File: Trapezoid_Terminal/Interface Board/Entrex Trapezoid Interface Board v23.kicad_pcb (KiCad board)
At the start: 2 copper layers, 169.1 x 191 mm, 101 parts, among them P15 Conn_02x40_Odd_Even_Shielded, SW1 SW_DIP_x08

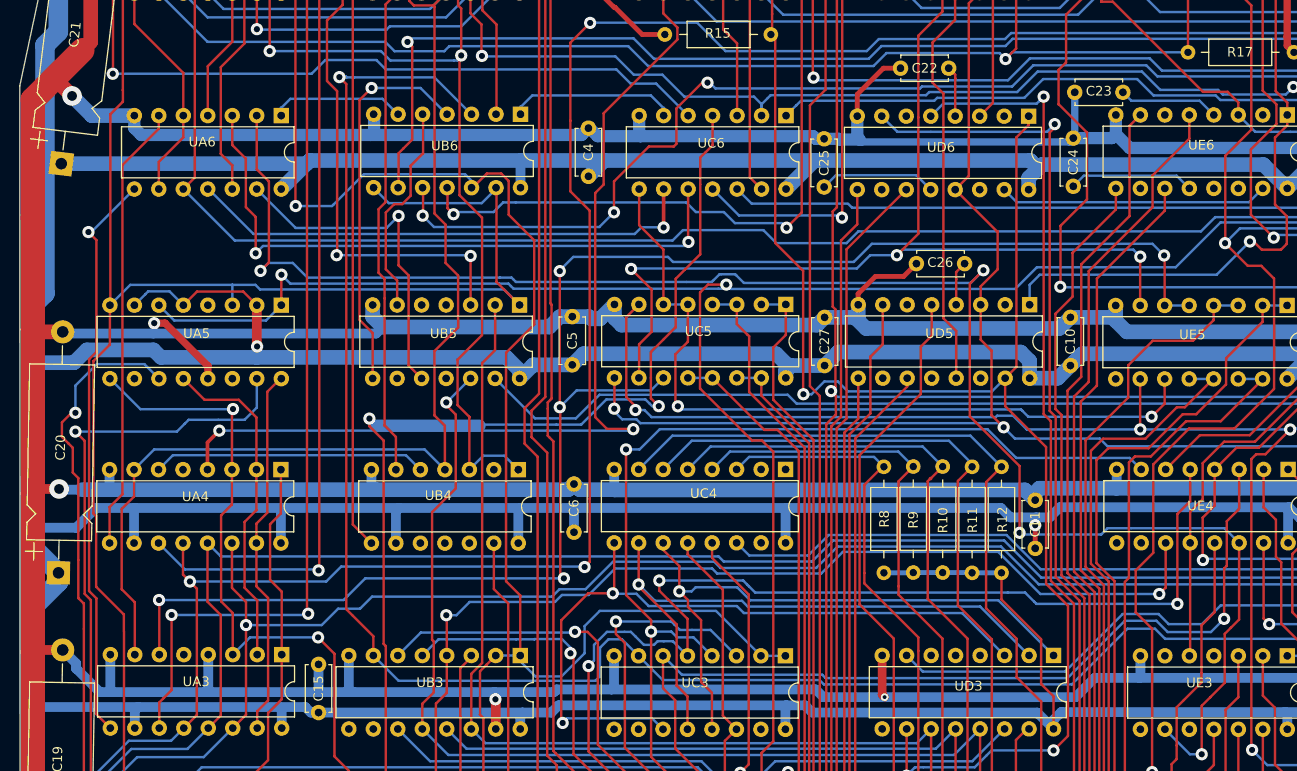
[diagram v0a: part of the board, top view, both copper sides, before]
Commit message: fix interface board errors
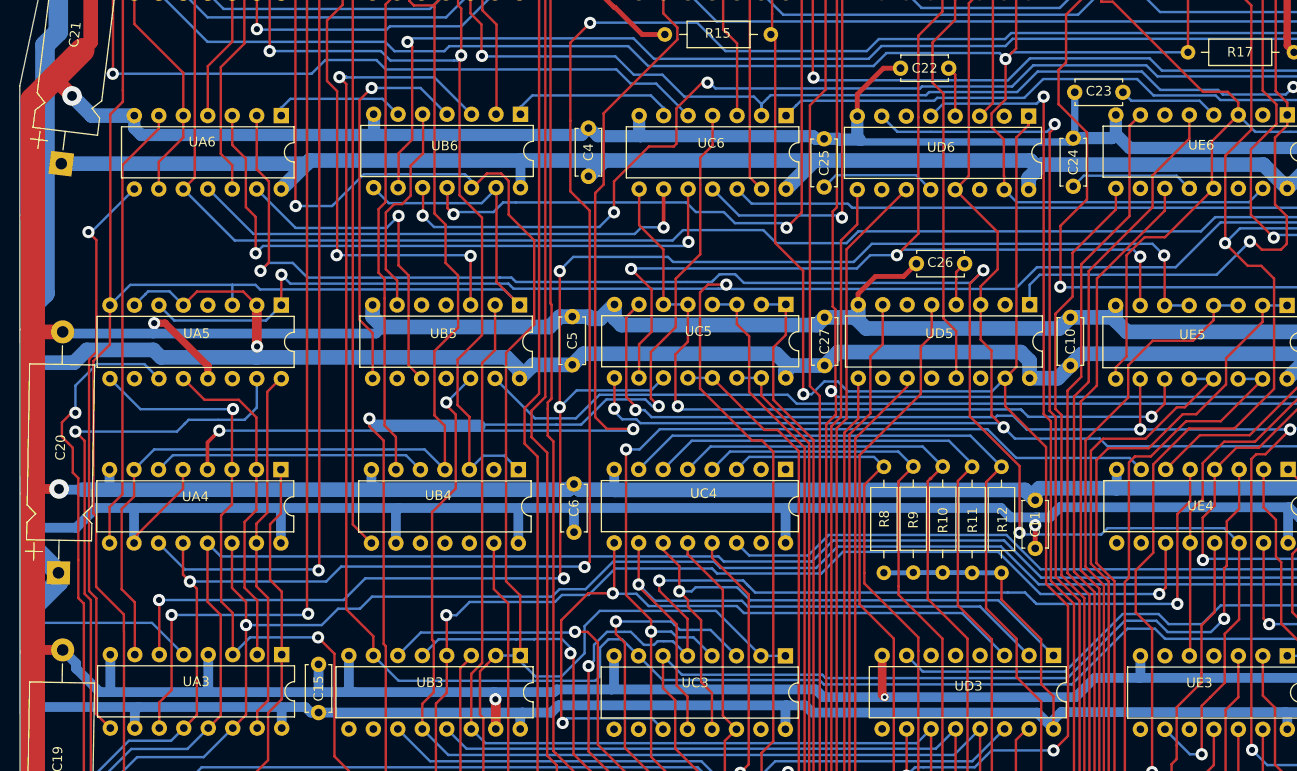
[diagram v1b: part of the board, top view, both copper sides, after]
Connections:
- UA3 pad 5: /XX(UA3P5) -> VCC
- UA4 pad 5: /XX(UA4P5) -> VCC
- UD6 pad 15: u16_15 -> u4_3
- UE5 pad 9: /XX(UE5P9) -> u4_2
- UE6 pad 13: unconnected-(UE6-2STRB-Pad13) -> u4_2
- UE6 pad 15: u16_15 -> u4_3
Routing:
- net u4_3: track 154.5 -> 197.2 mm
- net u4_2: track 214.8 -> 248.9 mm
- net u16_15: track 28.0 -> 0.00 mm
- net VCC: track 1844.7 -> 1871.5 mm

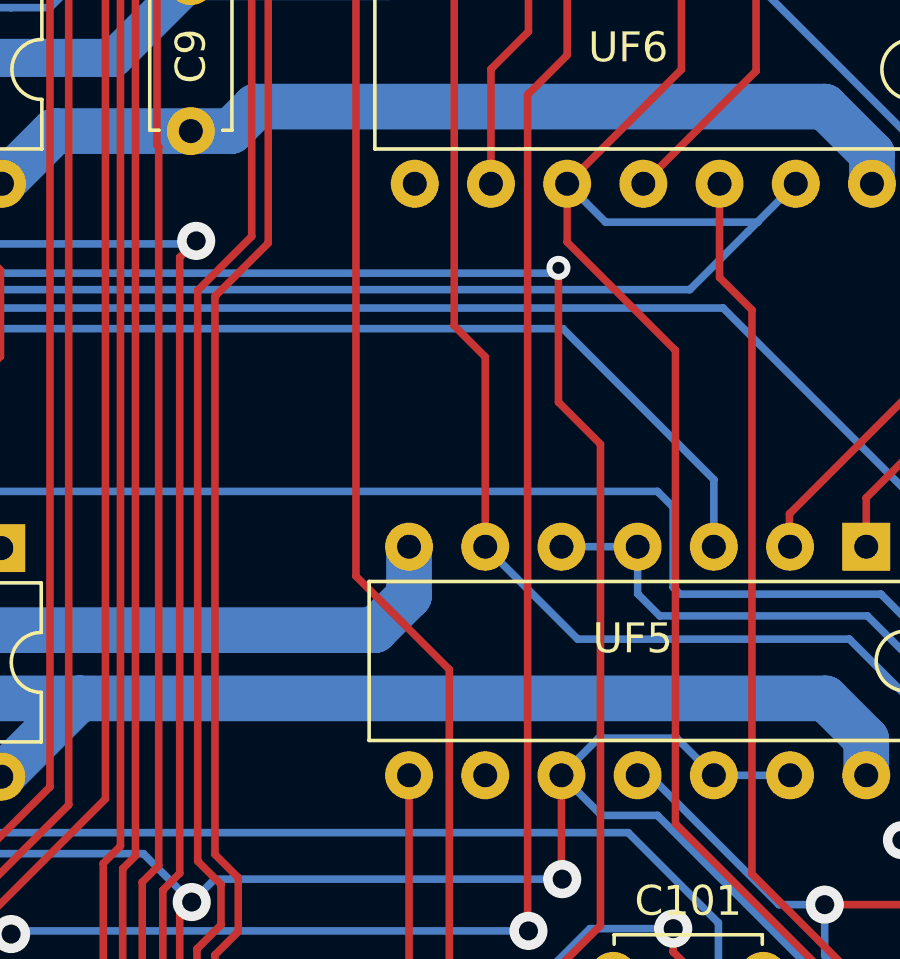
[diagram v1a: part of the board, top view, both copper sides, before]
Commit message: UF5 pin 9 connection
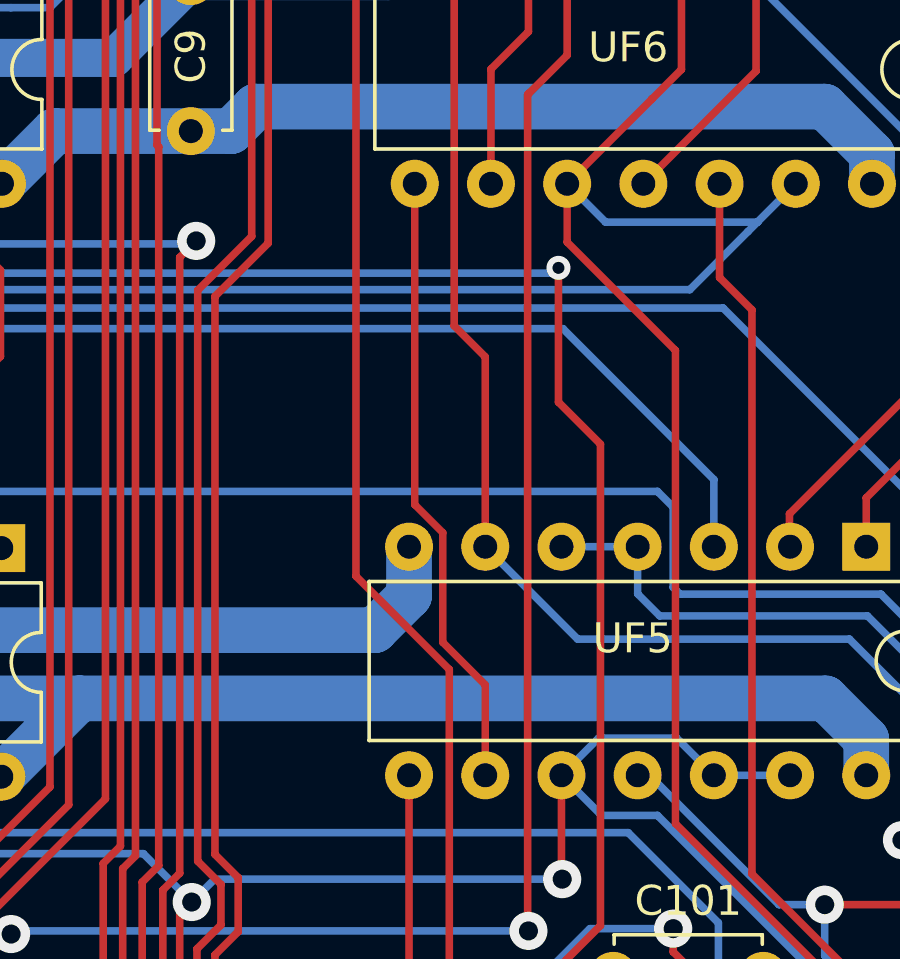
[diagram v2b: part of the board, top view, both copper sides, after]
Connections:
- UF5 pad 9: /XX(UF5P9) -> u18_8
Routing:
- net u18_8: track 0.00 -> 20.7 mm

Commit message: u34_13!
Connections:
- UA1 pad 14: u1_10 -> u34_13
- UA2 pad 14: u1_10 -> u34_13
- UA5 pad 3: u1_10 -> u34_13
- UA5 pad 8: u1_10 -> u34_13
- UA8 pad 10: u1_10 -> u34_13
- UB5 pad 1: u1_10 -> u34_13
- UB6 pad 13: u1_10 -> u34_13
- UB6 pad 8: u1_10 -> u34_13
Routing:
- net u34_13: track 292.1 -> 523.1 mm
- net u1_10: track 222.4 -> 0.00 mm

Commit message: u19_16/u19_12
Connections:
- C1 pad 2: VCC -> GND
- UA1 pad 16: u36_16 -> P15_11
- UA1 pad 17: P15_11 -> UA1_17
- UA2 pad 16: u36_16 -> P15_11
- UA3 pad 15: u19_16 -> P15_11
- UA3 pad 2: u19_12 -> P15_7
- UA4 pad 15: u19_16 -> P15_11
- UA4 pad 2: u19_12 -> P15_7
- UA5 pad 12: u19_12 -> P15_7
- UA5 pad 16: u19_16 -> P15_11
- UD1 pad 11: P15_11 -> UA1_17
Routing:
- net UA1_17: track 0.00 -> 80.5 mm
- net P15_7: track 57.0 -> 127.1 mm, vias 2 -> 3
- net u19_16: track 38.3 -> 0.00 mm
- net u19_12: track 34.9 -> 0.00 mm
- net u36_16: track 23.6 -> 0.00 mm
- net P15_11: track 127.2 -> 137.1 mm, vias 2 -> 3
- net GND: track 1624.3 -> 1625.1 mm

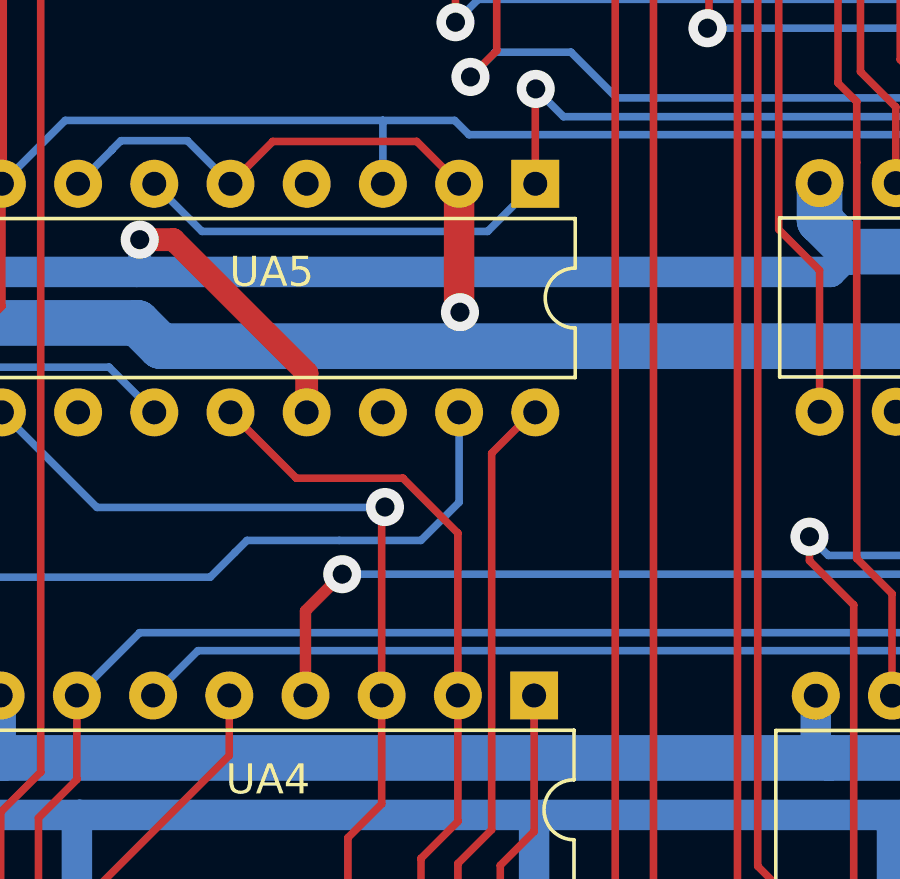
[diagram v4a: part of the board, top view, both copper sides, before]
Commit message: pin4 on UA5
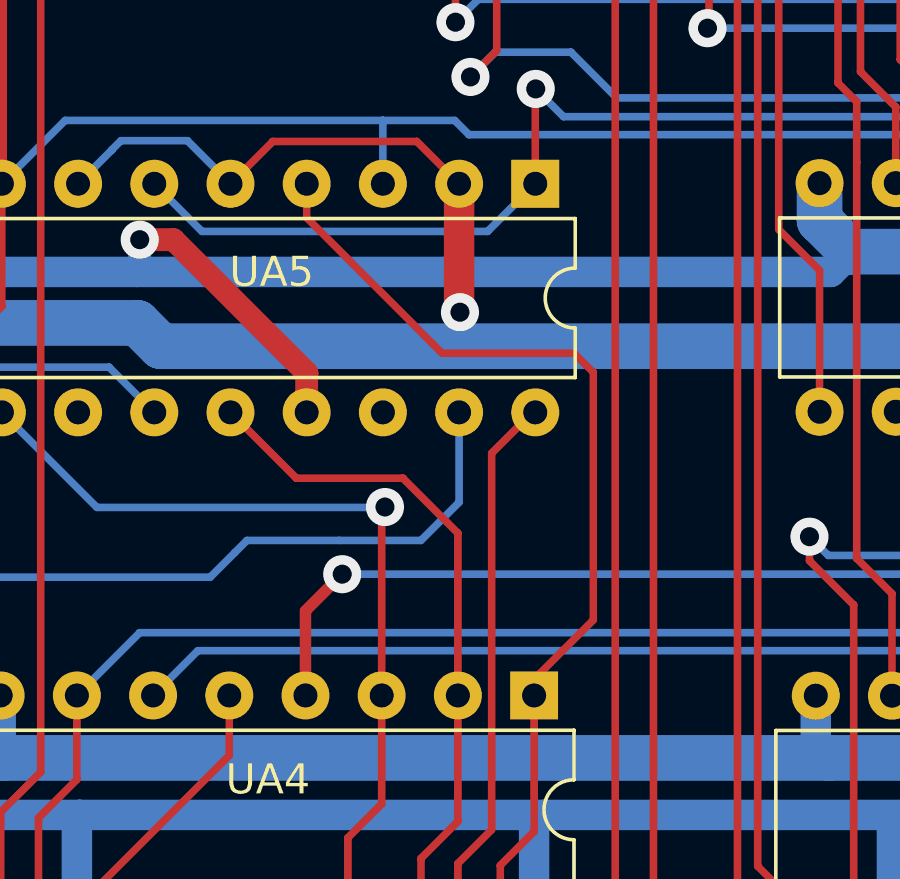
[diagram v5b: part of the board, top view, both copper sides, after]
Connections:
- UA5 pad 4: /XX(UA5P4) -> P15_9
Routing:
- net P15_9: track 117.4 -> 141.8 mm

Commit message: UB4
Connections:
- UB4 pad 10: unconnected-(UB4-Pad10) -> u8_11
- UB4 pad 2: unconnected-(UB4-Pad2) -> P15_19
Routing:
- net u8_11: track 379.1 -> 387.7 mm
- net P15_19: track 387.0 -> 394.6 mm

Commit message: fix
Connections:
- UA7 pad 3: /XX(UA7P3) -> u7-13
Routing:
- net u7-13: track 272.1 -> 280.8 mm

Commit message: UB8P12
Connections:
- UB8 pad 12: /XX(UB8P12) -> u2_10
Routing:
- net u2_10: track 92.4 -> 93.9 mm
